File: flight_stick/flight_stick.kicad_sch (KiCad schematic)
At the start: 54 parts, among them J1 Load Cell 1, J10 USB_C_Receptacle_USB2.0, J11 Conn_01x05_Pin, J3 Load Cell 2, J5 Load Cell 3, J7 Conn_01x04_Male, J8 Conn_01x05_Pin, J9 Conn_ST_STDC14, Q4 2N7002, Q5 2N7002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

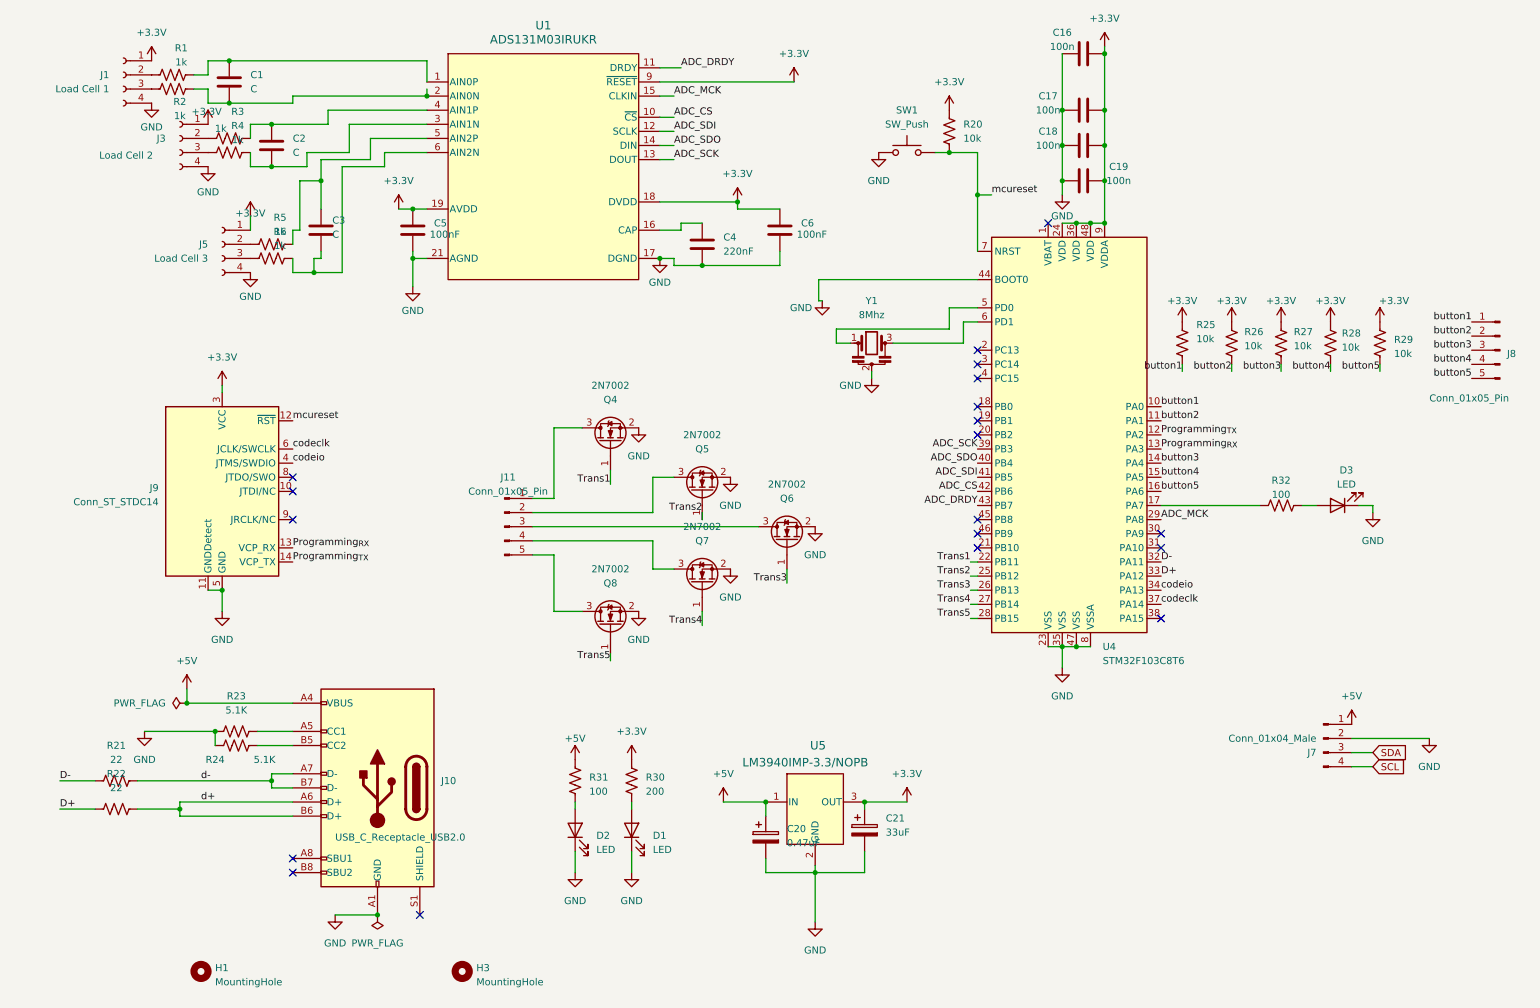
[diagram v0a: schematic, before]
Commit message: Reviewed Schematic and Assigned Footprints
Changed capacitor and resistor values
Checked all datasheets and made necessary connection changes
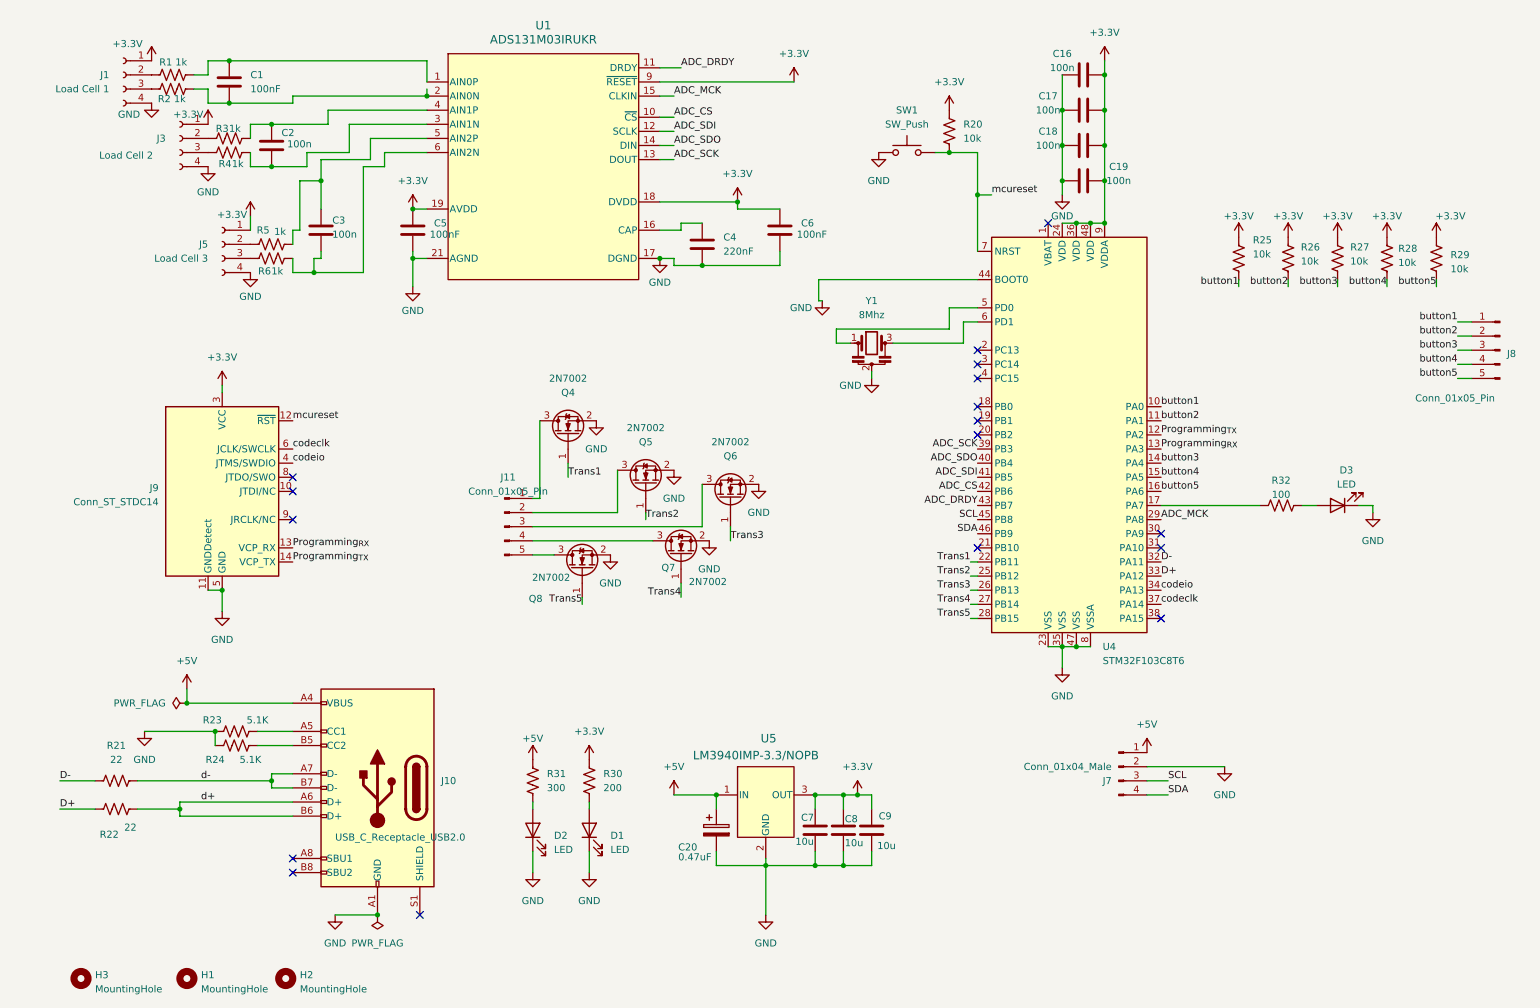
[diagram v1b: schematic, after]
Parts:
- removed C21: 33uF, Capacitor_SMD:C_0603_1608Metric, symbol Device:C_Polarized
- added C7, C8, C9: 10u, Capacitor_SMD:C_0603_1608Metric, symbol Device:C
- added H2: MountingHole, MountingHole:MountingHole_3.2mm_M3_ISO7380, symbol Mechanical:MountingHole
- C1: value C -> 100nF
- C2, C3: value C -> 100n
- R31: value 100 -> 300
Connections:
- net +3.3V: now also C7.1, C8.1, C9.1
- net AGND: now also C7.2, C8.2, C9.2
- net SCL: now also J7.3 (Pin_3), U4.45 (PB8); no longer J7.4 (Pin_4)
- net SDA: now also J7.4 (Pin_4), U4.46 (PB9); no longer J7.3 (Pin_3)
- no-connect marks 19 -> 17
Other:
- moved on the sheet: C16, C20, D1, D2, H1, H3, J7, Q4, Q5, Q6, Q7, Q8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

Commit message: Polishing up schematic
- Cleaned up libraries for parts/footprints
- Changed page and updated titleblock
- Changed symbol to reflect new microcontroller selection
- Updated symbols to modern KiCad variants
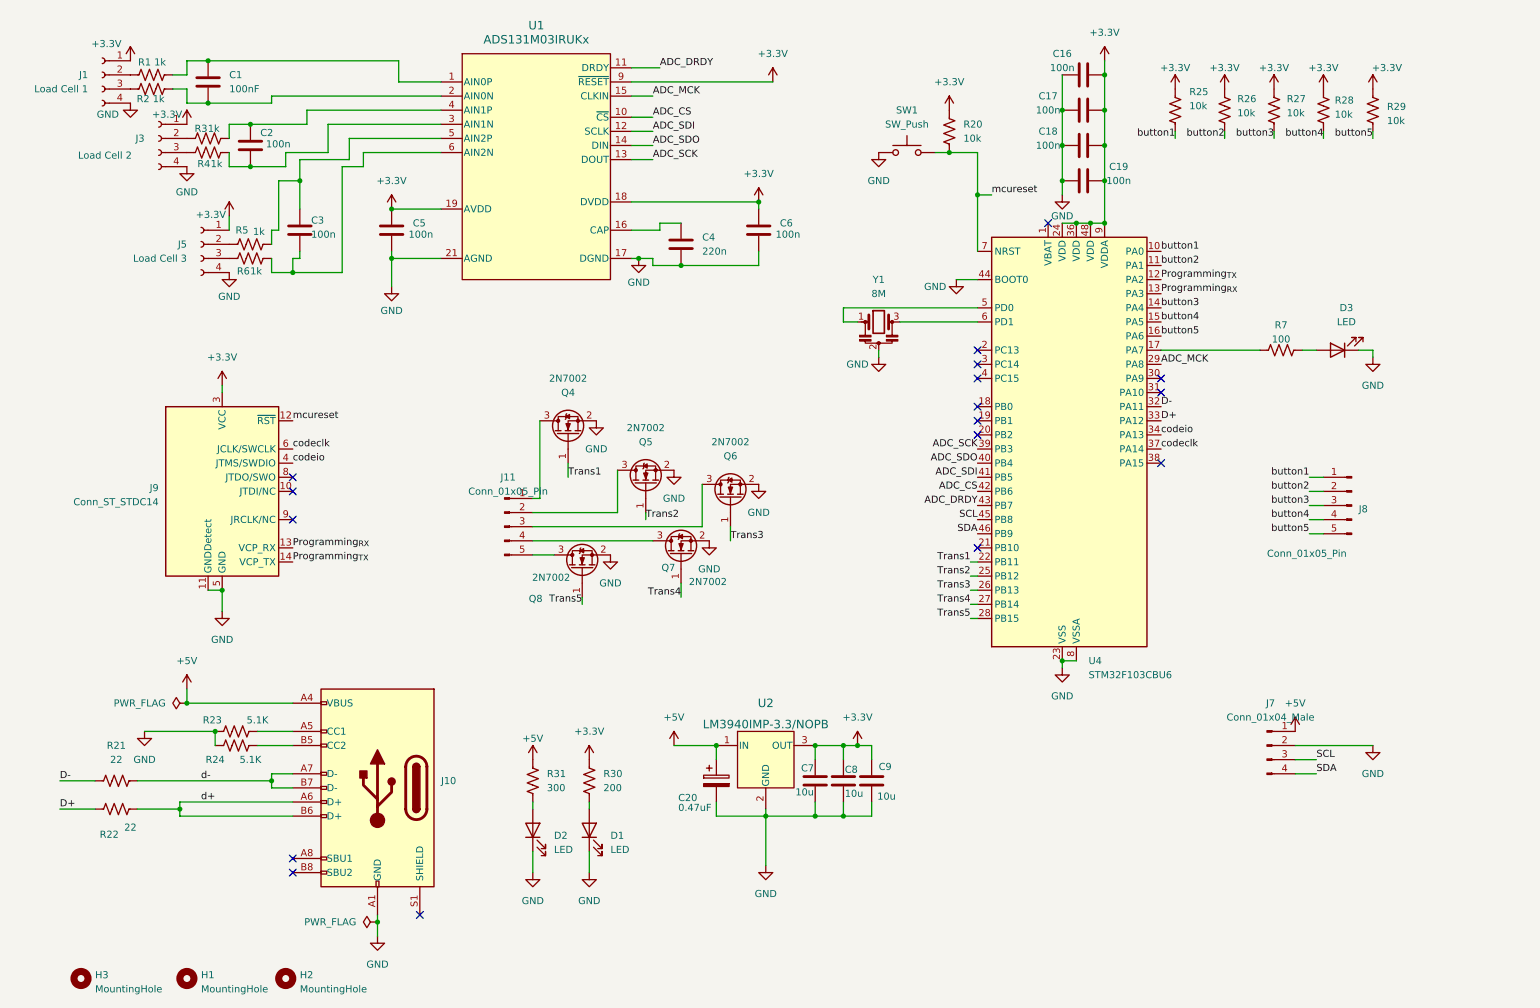
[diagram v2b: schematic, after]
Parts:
- removed R32: 100, Resistor_SMD:R_0603_1608Metric, symbol Device:R_US
- removed U1: ADS131M03IRUKR, ADS131M03 Footprint:QFN_WQFN_RUK_TEX, symbol 2024-07-27_18-32-59:ADS131M03IRUKR
- removed U5: LM3940IMP-3.3/NOPB, LFH_Voltagereg:MP04A, symbol 2024-03-22_01-04-52:LM3940IMP-3.3_NOPB
- added R7: 100, Resistor_SMD:R_0603_1608Metric, symbol Device:R_US
- added U1: ADS131M03IRUKx, flight_stick_footprints:QFN_WQFN_RUK_TEX, symbol flight_stick:ADS131M03IRUKx
- added U2: LM3940IMP-3.3/NOPB, flight_stick_footprints:MP04A, symbol flight_stick:LM3940IMP-3.3_NOPB
- C4: value 220nF -> 220n
- C5, C6: value 100nF -> 100n
- J1, J3, J5: symbol Connector:Conn_01x04_Female -> Connector:Conn_01x04_Socket; now in the parts list
- J10: symbol Connector:USB_C_Receptacle_USB2.0 -> Connector:USB_C_Receptacle_USB2.0_16P
- J7: symbol Connector:Conn_01x04_Male -> Connector:Conn_01x04_Pin
- U4: value STM32F103C8T6 -> STM32F103CBU6; footprint STM32F103C8T6_UFQFPN48:QFN-48_EP_7.3x7.3_Pitch0.5mm -> Package_DFN_QFN:QFN-48-1EP_7x7mm_P0.5mm_EP5.6x5.6mm; symbol MCU_ST_STM32F1:STM32F103C8Tx -> MCU_ST_STM32F1:STM32F103CBUx
- Y1: value 8Mhz -> 8M
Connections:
- net +3.3V: now also U1.18 (DVDD), U1.19 (AVDD), U1.9 (~{RESET}), U2.3 (OUT)
- net +5V: now also U2.1 (IN)
- net ADC_CS: now also U1.10 (~{CS})
- net ADC_DRDY: now also U1.11 (DRDY)
- net ADC_MCK: now also U1.15 (CLKIN)
- net ADC_SCK: now also U1.13 (DOUT)
- net ADC_SDI: now also U1.12 (SCLK)
- net ADC_SDO: now also U1.14 (DIN)
- net AGND: now also U4.49 (VSS), U1.17 (DGND), U1.20 (AGND), U1.21 (AGND), U2.2 (GND), U2.4 (GND)
- net at C3.2, R5.2: now also U1.5 (AIN2P)
- net at C2.2, R3.2: now also U1.4 (AIN1P)
- net at U4.17 (PA7): now also R7.1
- net at C1.2, R1.2: now also U1.1 (AIN0P)
- net at C4.1: now also U1.16 (CAP)
- net at C1.1, R2.2: now also U1.2 (AIN0N)
- net at C2.1, R4.2: now also U1.3 (AIN1N)
- net at C3.1, R6.2: now also U1.6 (AIN2N)
- net at D3.2 (A): now also R7.2
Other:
- company: (none) -> Aryan Ghosh
- title: (none) -> Flight Stick
- moved on the sheet: C1, C2, C20, C3, C4, C5, C6, C7, C8, C9, J1, J3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

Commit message: Began Layout
Started Layout no routing
Added RGB LED
Changed footprints
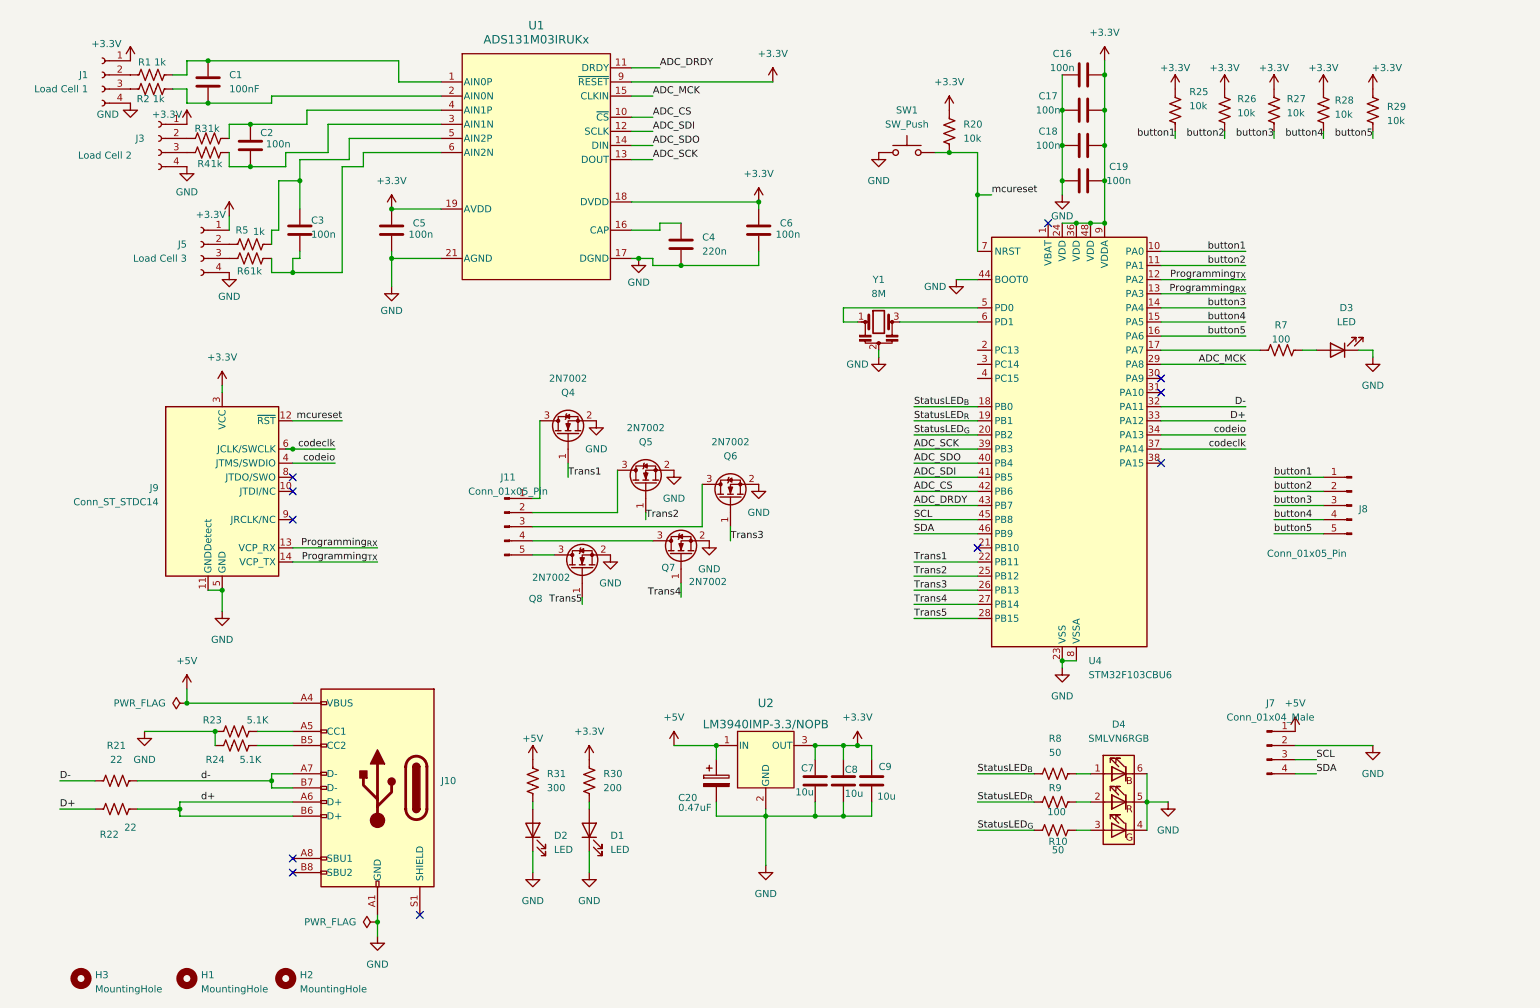
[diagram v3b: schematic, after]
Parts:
- added D4: SMLVN6RGB, LED_SMD:LED_ROHM_SMLVN6, symbol LED:SMLVN6RGB
- added R10, R8: 50, Resistor_SMD:R_0603_1608Metric, symbol Device:R_US
- added R9: 100, Resistor_SMD:R_0603_1608Metric, symbol Device:R_US
- J8: footprint Connector_PinHeader_2.54mm:PinHeader_1x05_P2.54mm_Horizontal -> Connector_PinHeader_2.54mm:PinHeader_1x05_P2.54mm_Vertical
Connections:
- net AGND: now also D4.4 (GK), D4.5 (RK), D4.6 (BK)
- net StatusLED_{B}: now reaches U4.18 (PB0)
- net StatusLED_{B}: now also R8.1
- net StatusLED_{R}: now reaches U4.19 (PB1)
- net StatusLED_{R}: now also R9.1
- net StatusLED_{G}: now reaches U4.20 (PB2)
- net StatusLED_{G}: now also R10.1
- new net: D4.3 (GA), R10.2
- new net: D4.2 (RA), R9.2
- new net: D4.1 (BA), R8.2
- no-connect marks 17 -> 11

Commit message: Finalized Component Placement
Finished Component Placement
Changed switch
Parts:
- SW1: footprint Button_Switch_SMD:SW_SPST_B3U-1000P-B -> Button_Switch_SMD:SW_Push_1P1T_NO_CK_KMR2
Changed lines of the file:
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@@
 			)
 		)
-		(property "Footprint" "Button_Switch_SMD:SW_SPST_B3U-1000P-B"
+		(property "Footprint" "Button_Switch_SMD:SW_Push_1P1T_NO_CK_KMR2"
 			(at 172.72 38.1 0)
 			(effects

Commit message: Started on the Routing
layout component placement requires review, traces placed
MCU pins re-assigned
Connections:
- net StatusLED_{B}: now also U4.20 (PB2); no longer U4.18 (PB0)
- net StatusLED_{G}: now also U4.18 (PB0); no longer U4.20 (PB2)
- net Trans1: now also U4.28 (PB15); no longer U4.22 (PB11)
- net Trans2: now also U4.27 (PB14); no longer U4.25 (PB12)
- net Trans4: now also U4.25 (PB12); no longer U4.27 (PB14)
- net Trans5: now also U4.22 (PB11); no longer U4.28 (PB15)
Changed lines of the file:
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@@
 		)
 	)
-	(label "Trans2"
-		(at 173.99 119.38 0)
+	(label "Trans1"
+		(at 173.99 127 0)
 		(fields_autoplaced yes)
 		(effects
@@
 		)
 	)
+	(label "StatusLED_{B}"
+		(at 173.99 93.98 0)
+		(fields_autoplaced yes)
+		(effects
+			(font
+				(size 1.27 1.27)
+			)
+			(justify left bottom)
+		)
+	)
 	(label "D-"
 		(at 20.32 156.21 0)
@@
 		)
 	)
-	(label "Trans4"
-		(at 173.99 124.46 0)
-		(fields_autoplaced yes)
-		(effects
-			(font
-				(size 1.27 1.27)
-			)
-			(justify left bottom)
-		)
-	)
 	(label "button5"
 		(at 233.68 76.2 180)
@@
 		)
 	)
+	(label "Trans2"
+		(at 173.99 124.46 0)
+		(fields_autoplaced yes)
+		(effects
+			(font
+				(size 1.27 1.27)
+			)
+			(justify left bottom)
+		)
+	)
 	(label "D-"
 		(at 233.68 88.9 180)
@@
 	)
 	(label "Trans1"
-		(at 173.99 116.84 0)
-		(fields_autoplaced yes)
-		(effects
-			(font
-				(size 1.27 1.27)
-			)
-			(justify left bottom)
-		)
-	)
-	(label "Trans1"
 		(at 111.76 101.6 0)
 		(fields_autoplaced yes)
@@
 		)
 	)
+	(label "Trans5"
+		(at 173.99 116.84 0)
+		(fields_autoplaced yes)
+		(effects
+			(font
+				(size 1.27 1.27)
+			)
+			(justify left bottom)
+		)
+	)
 	(label "button2"
 		(at 233.68 63.5 180)
@@
 		)
 	)
+	(label "Trans4"
+		(at 173.99 119.38 0)
+		(fields_autoplaced yes)
+		(effects
+			(font
+				(size 1.27 1.27)
+			)
+			(justify left bottom)
+		)
+	)
 	(label "D+"
 		(at 20.32 161.29 0)
@@
 		)
 	)
-	(label "StatusLED_{G}"
-		(at 173.99 93.98 0)
-		(fields_autoplaced yes)
-		(effects
-			(font
-				(size 1.27 1.27)
-			)
-			(justify left bottom)
-		)
-	)
 	(label "ADC_CS"
 		(at 173.99 104.14 0)
@@
 		)
 	)
-	(label "Trans5"
-		(at 173.99 127 0)
-		(fields_autoplaced yes)
-		(effects
-			(font
-				(size 1.27 1.27)
-			)
-			(justify left bottom)
-		)
-	)
 	(label "Programming_{RX}"
 		(at 233.68 68.58 180)
@@
 		)
 	)
+	(label "StatusLED_{G}"
+		(at 173.99 88.9 0)
+		(fields_autoplaced yes)
+		(effects
+			(font
+				(size 1.27 1.27)
+			)
+			(justify left bottom)
+		)
+	)
 	(label "ADC_SDO"
 		(at 127 41.91 0)
@@
 		)
 	)
-	(label "StatusLED_{B}"
-		(at 173.99 88.9 0)
-		(fields_autoplaced yes)
-		(effects
-			(font
-				(size 1.27 1.27)
-			)
-			(justify left bottom)
-		)
-	)
